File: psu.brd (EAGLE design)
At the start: 97.8 x 78.7 mm, 39 parts, among them IC1 7815T, IC2 7915T, IC3 7812T, IC4 7912T, IC5 7805T, J1 15VAC, J2 POWER_SW

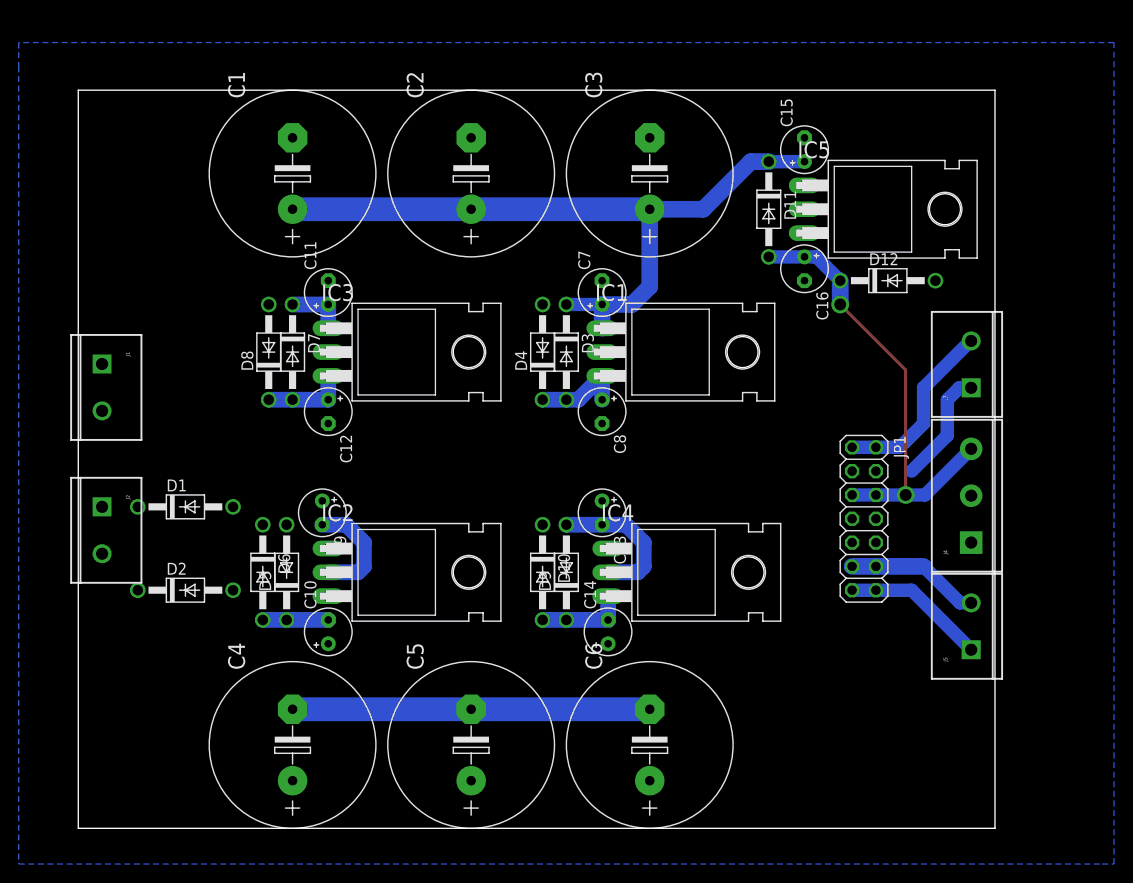
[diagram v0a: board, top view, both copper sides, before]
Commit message: Finish the board layout
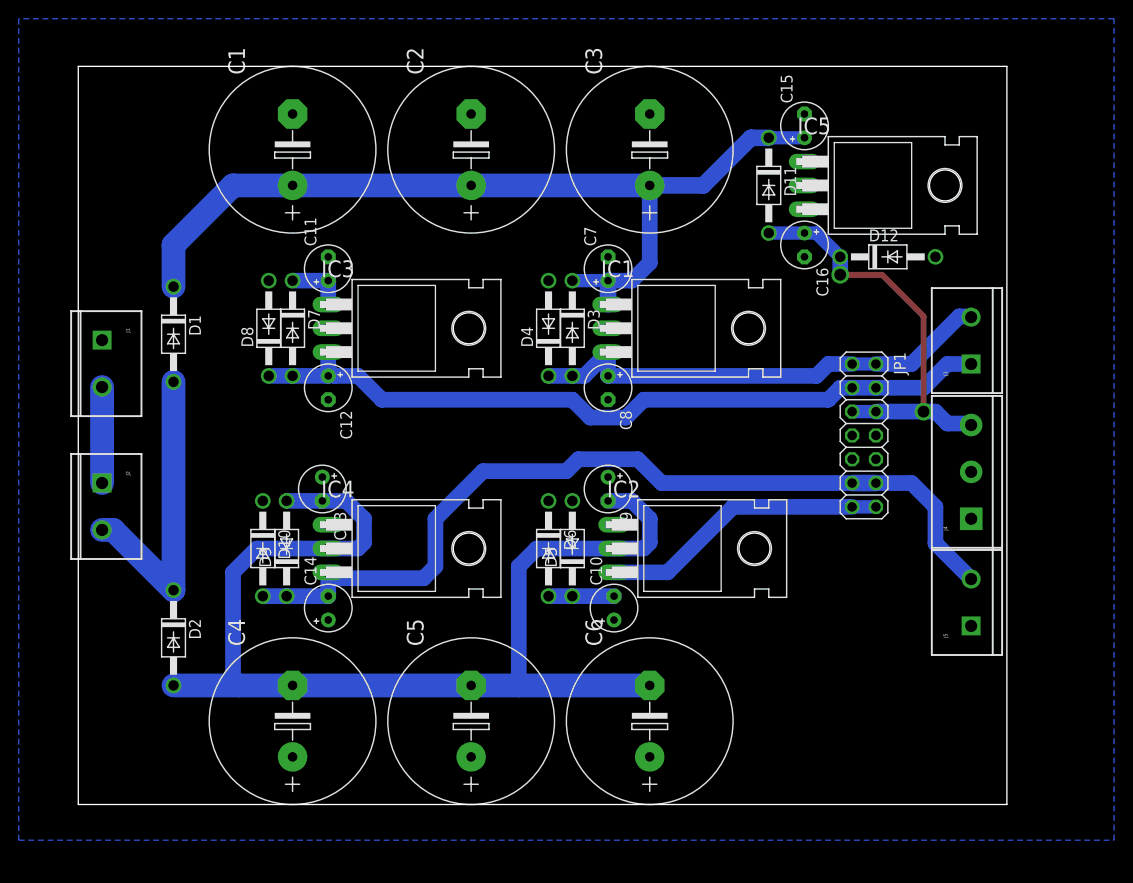
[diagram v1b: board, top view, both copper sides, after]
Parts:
- moved IC2 30.6 mm to (67.3, 27.3)
- moved C9 30.6 mm to (56.5, 33.7)
- moved D6 30.6 mm to (50.2, 27.3)
- moved C10 30.6 mm to (57.1, 21.0)
- moved D5 30.6 mm to (52.7, 27.3)
- moved C13 30.0 mm to (26.0, 33.7)
- moved D10 30.0 mm to (19.7, 27.3)
- moved C14 30.0 mm to (26.7, 21.0)
- moved D9 30.0 mm to (22.2, 27.3)
- moved IC4 30.0 mm to (36.8, 27.3)
- moved D1 18.5 mm to (10.2, 50.2), turned to 270 degrees
- moved JP1 8.89 mm to (83.8, 39.4)
- moved D2 5.24 mm to (10.2, 17.8), turned to 270 degrees
- moved C8 2.62 mm to (56.5, 44.5)
- moved C7 2.62 mm to (56.5, 57.1)
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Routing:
- net -12V: track 23.8 -> 94.2 mm
- net +12V: track 21.2 -> 81.9 mm
- net -AC: track 65.6 -> 125.5 mm
- net N$2: track 0.00 -> 32.5 mm
- net +15V: track 29.6 -> 51.3 mm
- net +AC: track 83.5 -> 102.7 mm
- net -15V: track 22.3 -> 37.8 mm
- net N$1: track 0.00 -> 10.2 mm
- net +5V: track 49.2 -> 44.8 mm
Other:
- board size 97.8 x 78.7 mm -> 99.1 x 78.7 mm

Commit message: Final version of psu, I guess?
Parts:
- moved C14 0.64 mm to (26.0, 21.0)
- moved C9 0.63 mm to (57.1, 33.7)
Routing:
- net -15V: track 37.8 -> 59.5 mm
- net GND: track 0.00 -> 15.9 mm, vias 0 -> 2
- net +AC: track 102.7 -> 117.4 mm
- net -AC: track 125.5 -> 133.4 mm
- net -12V: track 94.2 -> 94.8 mm
